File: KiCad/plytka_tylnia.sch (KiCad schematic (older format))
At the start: 91 parts, among them J1 CONN_01X04, J2 CONN_01X04, J3 CONN_01X04, J4 CONN_01X04, J5 CONN_01X04, J6 CONN_01X04, J7 PIN10, J8 CONN_01X04, J9 CONN_01X04, P1 USB_OTG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

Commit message: zmienione przelotki na 1,4/0,5
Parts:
- removed BATERIA?: LI-POL, misc:zl_zasilania, symbol CONN_01X02
- removed Bezpiecznik?: Fuse ??, Fuse_Holders_and_Fuses:Fuse_SMD1206_HandSoldering, symbol Fuse
- removed C? (x2): 10uF, Capacitors_Tantalum_SMD:CP_Tantalum_Case-A_EIA-3216-18_Hand, symbol CP
- removed J?: CONN_02X20, symbol CONN_02X20
- removed J? (x2): CONN_01X20, symbol CONN_01X20
- removed R?: 1k, Resistors_SMD:R_0805_HandSoldering, symbol R
- removed STABILIZATOR?: LM1117, warsztaty:LM1117_TO-252, symbol LM1117
- removed TRANSISTOR?: BUZ11, misc:SOT23-3, symbol BUZ11
- removed Włącznik?: switch, misc:tact_switch_smd, symbol SPST
- renumbered C15 to C1.1
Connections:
- net labels added: L_1, L_2, R_1, R_2, T1P, T2P, T3P, T4P, T5P, T6P, T7P, T8P
- net labels removed: GND3, L_IN1, L_IN2, PWM5V, R_IN1, R_IN2, VCC3
- wire segments 187 -> 169
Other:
- moved on the sheet: C1.1, C1.2, C16, C18, C2.1, C2.2, J1, J2, J3, J4, J5, J6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

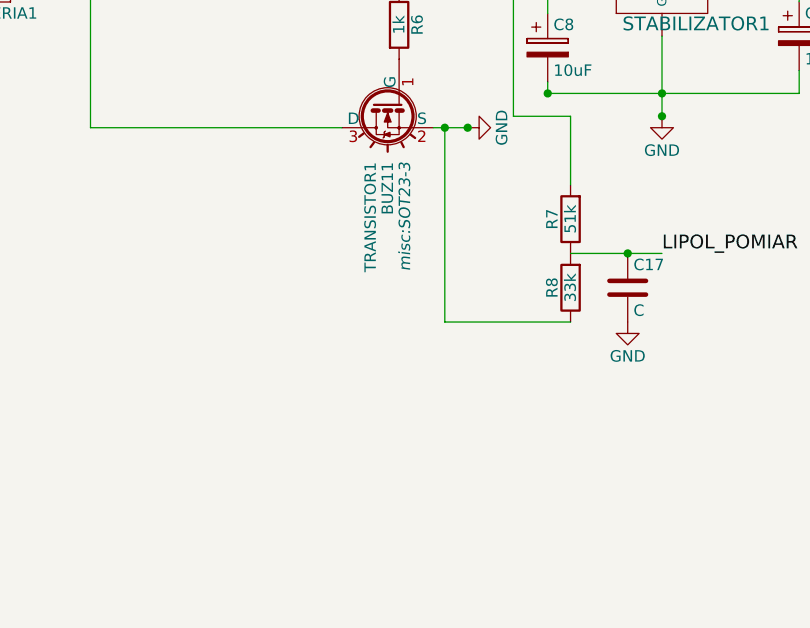
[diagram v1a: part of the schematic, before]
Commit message: raster goldpin na 2,54, scieżki wokół procka i mostka na 0,3 mm,
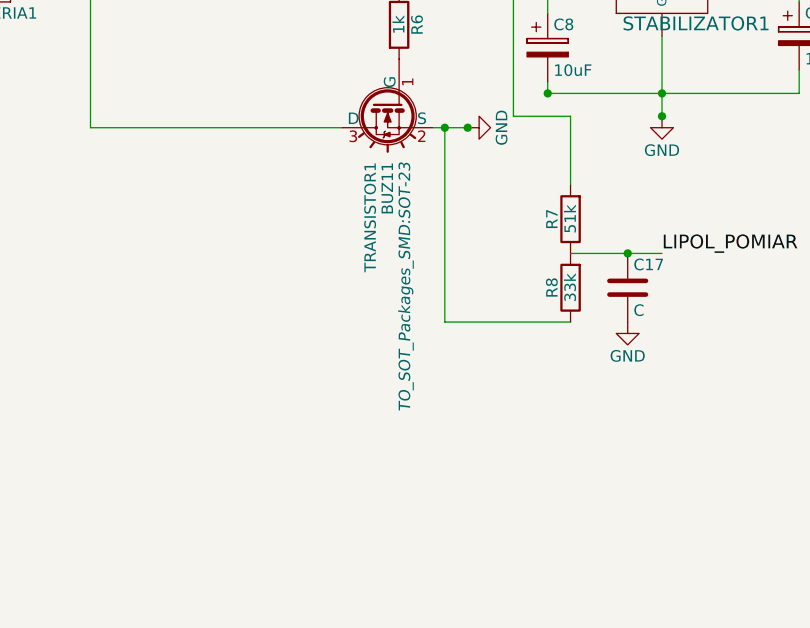
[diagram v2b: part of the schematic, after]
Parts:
- BLUETOOTH1, J1, J2, J3, J4, J5, J6, J8, J9: footprint Pin_Headers:Pin_Header_Straight_1x04_Pitch2.00mm -> 111:GoldPin_1x4
- TRANSISTOR1: footprint misc:SOT23-3 -> TO_SOT_Packages_SMD:SOT-23
- Włącznik1: footprint misc:tact_switch_smd -> misc:dip_switch_1
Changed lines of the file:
@@
 F 0 "TRANSISTOR1" H 3400 13325 50  0000 L CNN
 F 1 "BUZ11" H 3400 13250 50  0000 L CNN
-F 2 "misc:SOT23-3" H 3400 13175 50  0000 L CIN
+F 2 "TO_SOT_Packages_SMD:SOT-23" H 3400 13175 50  0000 L CIN
 F 3 "" H 3150 13250 50  0000 L CNN
 	1    3150 13250
@@
 F 0 "BLUETOOTH1" H 4650 9300 50  0000 C CNN
 F 1 "PIN4" V 4750 9050 50  0000 C CNN
-F 2 "Pin_Headers:Pin_Header_Straight_1x04_Pitch2.00mm" H 4650 9050 50  0001 C CNN
+F 2 "111:GoldPin_1x4" H 4650 9050 50  0001 C CNN
 F 3 "" H 4650 9050 50  0000 C CNN
 	1    4650 9050
@@
 F 0 "Włącznik1" H 2150 12750 50  0000 C CNN
 F 1 "switch" H 2150 12550 50  0000 C CNN
-F 2 "misc:tact_switch_smd" H 2150 12650 50  0001 C CNN
+F 2 "misc:dip_switch_1" H 2150 12650 50  0001 C CNN
 F 3 "" H 2150 12650 50  0000 C CNN
 	1    2150 12650
@@
 F 0 "J1" H 18900 8000 50  0000 C CNN
 F 1 "CONN_01X04" V 19000 7750 50  0000 C CNN
-F 2 "Pin_Headers:Pin_Header_Straight_1x04_Pitch2.00mm" H 18900 7750 50  0001 C CNN
+F 2 "111:GoldPin_1x4" H 18900 7750 50  0001 C CNN
 F 3 "" H 18900 7750 50  0001 C CNN
 	1    18900 7750
@@
 F 0 "J2" H 18900 8550 50  0000 C CNN
 F 1 "CONN_01X04" V 19000 8300 50  0000 C CNN
-F 2 "Pin_Headers:Pin_Header_Straight_1x04_Pitch2.00mm" H 18900 8300 50  0001 C CNN
+F 2 "111:GoldPin_1x4" H 18900 8300 50  0001 C CNN
 F 3 "" H 18900 8300 50  0001 C CNN
 	1    18900 8300
@@
 F 0 "J3" H 21000 8050 50  0000 C CNN
 F 1 "CONN_01X04" V 21100 7800 50  0000 C CNN
-F 2 "Pin_Headers:Pin_Header_Straight_1x04_Pitch2.00mm" H 21000 7800 50  0001 C CNN
+F 2 "111:GoldPin_1x4" H 21000 7800 50  0001 C CNN
 F 3 "" H 21000 7800 50  0001 C CNN
 	1    21000 7800
@@
 F 0 "J4" H 21000 8600 50  0000 C CNN
 F 1 "CONN_01X04" V 21100 8350 50  0000 C CNN
-F 2 "Pin_Headers:Pin_Header_Straight_1x04_Pitch2.00mm" H 21000 8350 50  0001 C CNN
+F 2 "111:GoldPin_1x4" H 21000 8350 50  0001 C CNN
 F 3 "" H 21000 8350 50  0001 C CNN
 	1    21000 8350
@@
 F 0 "J9" H 20800 10550 50  0000 C CNN
 F 1 "CONN_01X04" V 20900 10300 50  0000 C CNN
-F 2 "Pin_Headers:Pin_Header_Straight_1x04_Pitch2.00mm" H 20800 10300 50  0001 C CNN
+F 2 "111:GoldPin_1x4" H 20800 10300 50  0001 C CNN
 F 3 "" H 20800 10300 50  0001 C CNN
 	1    20800 10300
@@
 F 0 "J6" H 19050 10600 50  0000 C CNN
 F 1 "CONN_01X04" V 19150 10350 50  0000 C CNN
-F 2 "Pin_Headers:Pin_Header_Straight_1x04_Pitch2.00mm" H 19050 10350 50  0001 C CNN
+F 2 "111:GoldPin_1x4" H 19050 10350 50  0001 C CNN
 F 3 "" H 19050 10350 50  0001 C CNN
 	1    19050 10350
@@
 F 0 "J5" H 19050 9850 50  0000 C CNN
 F 1 "CONN_01X04" V 19150 9600 50  0000 C CNN
-F 2 "Pin_Headers:Pin_Header_Straight_1x04_Pitch2.00mm" H 19050 9600 50  0001 C CNN
+F 2 "111:GoldPin_1x4" H 19050 9600 50  0001 C CNN
 F 3 "" H 19050 9600 50  0001 C CNN
 	1    19050 9600
@@
 F 0 "J8" H 20750 9800 50  0000 C CNN
 F 1 "CONN_01X04" V 20850 9550 50  0000 C CNN
-F 2 "Pin_Headers:Pin_Header_Straight_1x04_Pitch2.00mm" H 20750 9550 50  0001 C CNN
+F 2 "111:GoldPin_1x4" H 20750 9550 50  0001 C CNN
 F 3 "" H 20750 9550 50  0001 C CNN
 	1    20750 9550
